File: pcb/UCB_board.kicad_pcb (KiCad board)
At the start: 4 copper layers, 160 x 100 mm, 159 parts, among them IC1 SN65HVD75DR, J1 DIN41612_02x32_AC, J2 TC2030, J3 Conn_01x02_Pin, T1 H1102NL, U1 W5500, U2 LM4040DBZ-3, U3 USBLC6-2SC6, U4 USBLC6-2SC6, U5 USBLC6-2SC6, U6 FM24C64B, U7 STM32H563VITx, Y1 3225-25M-SR, Y2 3225-25M-SR

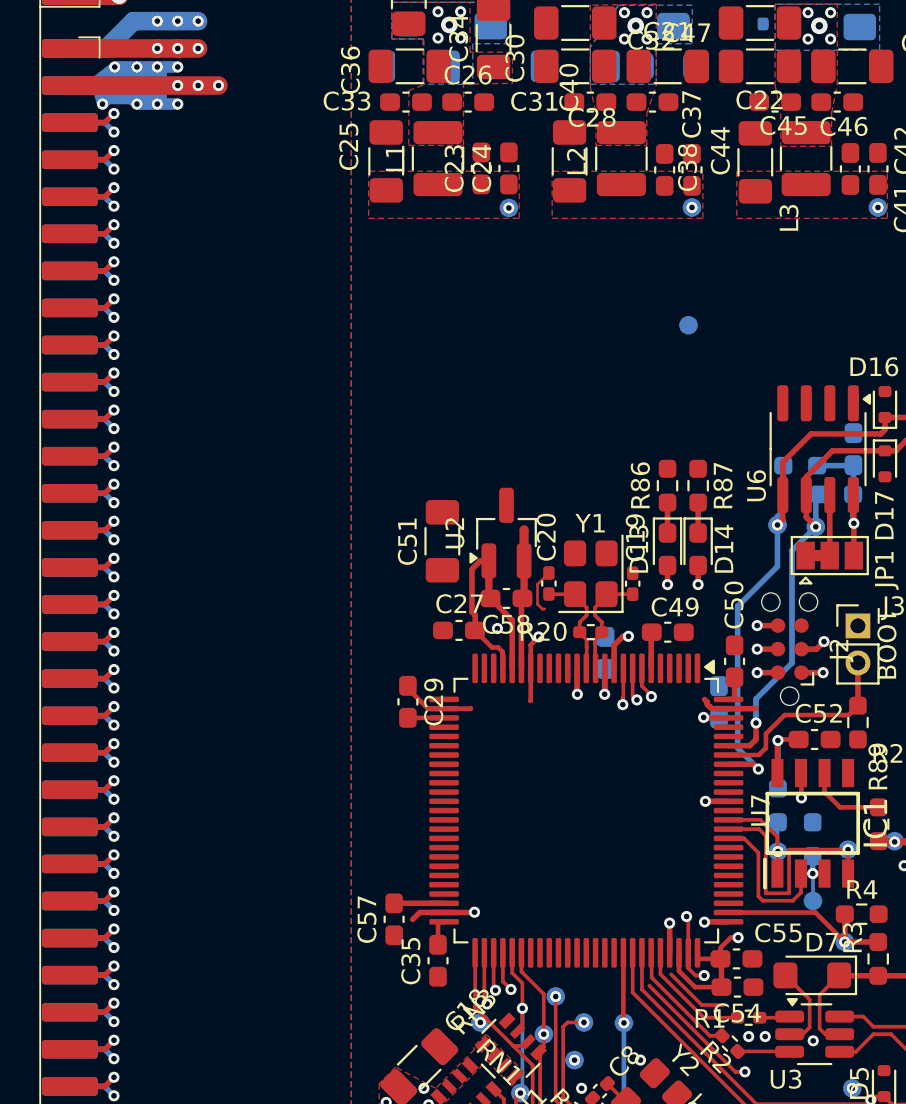
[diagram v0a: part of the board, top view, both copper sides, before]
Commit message: UniConnector new traces
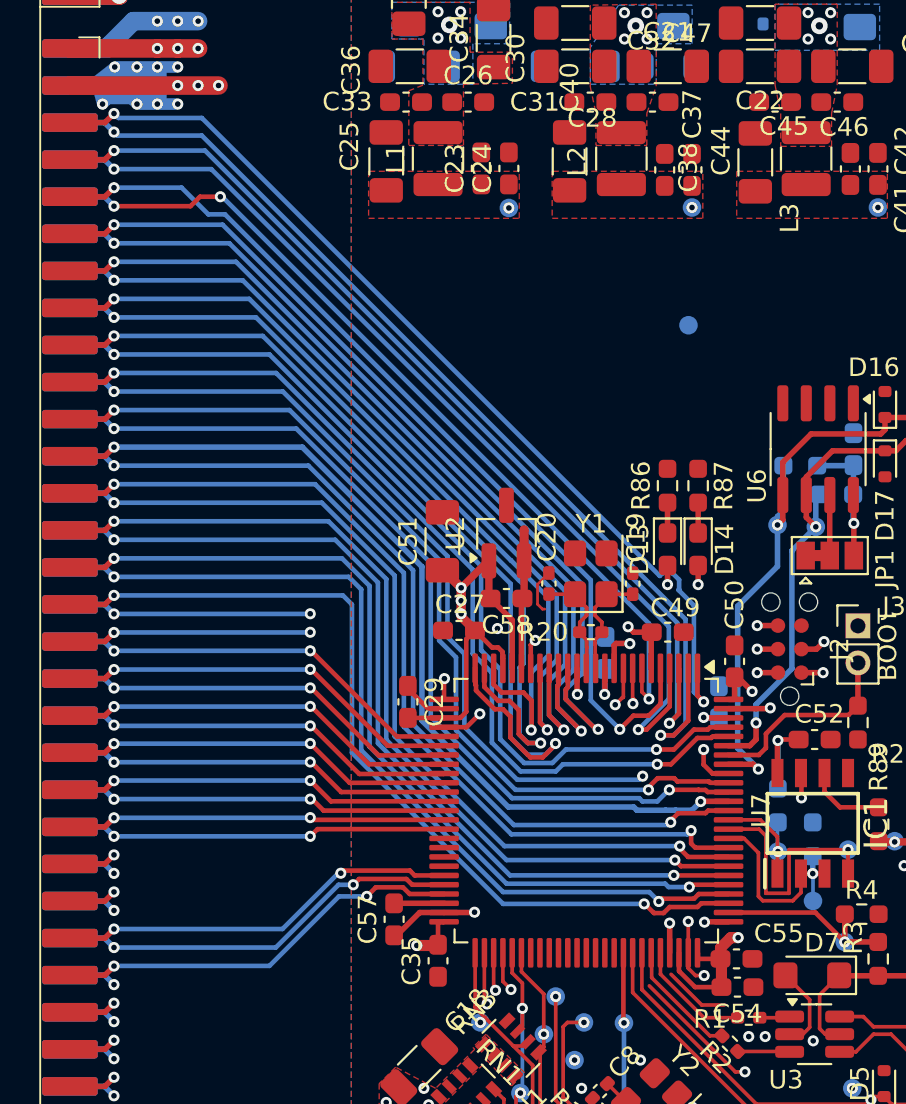
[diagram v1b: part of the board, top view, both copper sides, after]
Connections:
- net /UniConnector/IO_48 renamed /MCU/IO_48
- net /UniConnector/IO_49 renamed /MCU/IO_49
- net /UniConnector/IO_50 renamed /MCU/IO_50
- net /UniConnector/IO_51 renamed /MCU/IO_51
- net /UniConnector/IO_52 renamed /MCU/IO_52
- net /UniConnector/IO_53 renamed /MCU/IO_53
- net /UniConnector/IO_54 renamed /MCU/IO_54
- net /UniConnector/IO_55 renamed /MCU/IO_55
- net /UniConnector/IO_56 renamed /MCU/IO_56
- net /UniConnector/IO_57 renamed /MCU/IO_57
- net /UniConnector/IO_58 renamed /MCU/IO_58
- net /UniConnector/IO_59 renamed /MCU/IO_59
- net /UniConnector/IO_60 renamed /MCU/IO_60
- net /UniConnector/IO_61 renamed /MCU/IO_61
- net /UniConnector/IO_62 renamed /MCU/IO_62
- net /UniConnector/IO_63 renamed /MCU/IO_63
- net /UniConnector/IO_64 renamed /MCU/IO_64
- net /UniConnector/IO_65 renamed /MCU/IO_65
- net /UniConnector/IO_66 renamed /MCU/IO_66
- net /UniConnector/IO_67 renamed /MCU/IO_67
- net /UniConnector/IO_68 renamed /MCU/IO_68
- net /UniConnector/IO_69 renamed /MCU/IO_69
- net /UniConnector/IO_70 renamed /MCU/IO_70
- net /UniConnector/IO_71 renamed /MCU/IO_71
- net /UniConnector/IO_72 renamed /MCU/IO_72
- net /UniConnector/IO_73 renamed /MCU/IO_73
- net /UniConnector/IO_74 renamed /MCU/IO_74
- net /UniConnector/IO_75 renamed /MCU/IO_75
- net /UniConnector/IO_76 renamed /MCU/IO_76
- J2 pad 4: /MCU/IO_20 -> /MCU/IO_19
- U7 pad 26: /MCU/IO_14 -> /MCU/IO_28
- U7 pad 29: unconnected-(U7-PA4-Pad29) -> /MCU/IO_29
- U7 pad 30: unconnected-(U7-PA5-Pad30) -> /MCU/IO_30
- U7 pad 31: unconnected-(U7-PA6-Pad31) -> /MCU/IO_31
- U7 pad 32: unconnected-(U7-PA7-Pad32) -> /MCU/IO_32
- U7 pad 33: unconnected-(U7-PC4-Pad33) -> /MCU/IO_33
- U7 pad 34: unconnected-(U7-PC5-Pad34) -> /MCU/IO_34
- U7 pad 35: unconnected-(U7-PB0-Pad35) -> /MCU/IO_35
- U7 pad 36: unconnected-(U7-PB1-Pad36) -> /MCU/IO_36
- U7 pad 37: unconnected-(U7-PB2-Pad37) -> /MCU/IO_37
- U7 pad 38: unconnected-(U7-PE7-Pad38) -> /MCU/IO_38
- U7 pad 39: unconnected-(U7-PE8-Pad39) -> /MCU/IO_39
- U7 pad 40: unconnected-(U7-PE9-Pad40) -> /MCU/IO_40
- U7 pad 41: unconnected-(U7-PE10-Pad41) -> /MCU/IO_41
- U7 pad 42: unconnected-(U7-PE11-Pad42) -> /MCU/IO_42
- U7 pad 43: unconnected-(U7-PE12-Pad43) -> /MCU/IO_43
- U7 pad 44: unconnected-(U7-PE13-Pad44) -> /MCU/IO_44
- U7 pad 45: unconnected-(U7-PE14-Pad45) -> /MCU/IO_45
- U7 pad 46: unconnected-(U7-PE15-Pad46) -> /MCU/IO_46
- U7 pad 47: unconnected-(U7-PB10-Pad47) -> /MCU/IO_47
- U7 pad 78: /MCU/IO_28 -> /MCU/IO_27
- U7 pad 79: /MCU/IO_27 -> /MCU/IO_26
- U7 pad 80: /MCU/IO_26 -> /MCU/IO_25
- U7 pad 81: /MCU/IO_25 -> /MCU/IO_24
- U7 pad 82: /MCU/IO_24 -> /MCU/IO_23
- U7 pad 83: /MCU/IO_23 -> /MCU/IO_22
- U7 pad 84: /MCU/IO_22 -> /MCU/IO_21
- U7 pad 88: /MCU/IO_21 -> /MCU/IO_20
- U7 pad 89: /MCU/IO_20 -> /MCU/IO_19
- U7 pad 90: /MCU/IO_19 -> /MCU/IO_18
- U7 pad 91: /MCU/IO_18 -> /MCU/IO_17
- U7 pad 92: /MCU/IO_17 -> /MCU/IO_16
- U7 pad 96: /MCU/IO_16 -> /MCU/IO_15
- U7 pad 97: /MCU/IO_15 -> /MCU/IO_14
- X1 pad 10: /UniConnector/IO_6 -> /MCU/IO_6
- X1 pad 11: /UniConnector/IO_7 -> /MCU/IO_7
- X1 pad 12: /UniConnector/IO_8 -> /MCU/IO_8
- X1 pad 13: /UniConnector/IO_9 -> /MCU/IO_9
- X1 pad 14: /UniConnector/IO_10 -> /MCU/IO_10
- X1 pad 15: /UniConnector/IO_11 -> /MCU/IO_11
- X1 pad 16: /UniConnector/IO_12 -> /MCU/IO_12
- X1 pad 17: /UniConnector/IO_13 -> /MCU/IO_13
- X1 pad 18: /UniConnector/IO_14 -> /MCU/IO_14
- X1 pad 19: /UniConnector/IO_15 -> /MCU/IO_15
- X1 pad 20: /UniConnector/IO_16 -> /MCU/IO_16
- X1 pad 21: /UniConnector/IO_17 -> /MCU/IO_17
- X1 pad 22: /UniConnector/IO_18 -> /MCU/IO_18
- X1 pad 23: /UniConnector/IO_19 -> /MCU/IO_19
- X1 pad 24: /UniConnector/IO_20 -> /MCU/IO_20
- X1 pad 25: /UniConnector/IO_21 -> /MCU/IO_21
- X1 pad 26: /UniConnector/IO_22 -> /MCU/IO_22
- X1 pad 27: /UniConnector/IO_23 -> /MCU/IO_23
- X1 pad 28: /UniConnector/IO_24 -> /MCU/IO_24
- X1 pad 29: /UniConnector/IO_25 -> /MCU/IO_25
- X1 pad 30: /UniConnector/IO_26 -> /MCU/IO_26
- X1 pad 31: /UniConnector/IO_27 -> /MCU/IO_27
- X1 pad 32: /UniConnector/IO_28 -> /MCU/IO_28
- X1 pad 33: /UniConnector/IO_29 -> /MCU/IO_29
- X1 pad 34: /UniConnector/IO_30 -> /MCU/IO_30
- X1 pad 35: /UniConnector/IO_31 -> /MCU/IO_31
- X1 pad 36: /UniConnector/IO_32 -> /MCU/IO_32
- X1 pad 37: /UniConnector/IO_33 -> /MCU/IO_33
- X1 pad 38: /UniConnector/IO_34 -> /MCU/IO_34
- X1 pad 39: /UniConnector/IO_35 -> /MCU/IO_35
- X1 pad 40: /UniConnector/IO_36 -> /MCU/IO_36
- X1 pad 41: /UniConnector/IO_37 -> /MCU/IO_37
- X1 pad 42: /UniConnector/IO_38 -> /MCU/IO_38
- X1 pad 43: /UniConnector/IO_39 -> /MCU/IO_39
- X1 pad 44: /UniConnector/IO_40 -> /MCU/IO_40
- X1 pad 45: /UniConnector/IO_41 -> /MCU/IO_41
- X1 pad 46: /UniConnector/IO_42 -> /MCU/IO_42
- X1 pad 47: /UniConnector/IO_43 -> /MCU/IO_43
- X1 pad 48: /UniConnector/IO_44 -> /MCU/IO_44
- X1 pad 49: /UniConnector/IO_45 -> /MCU/IO_45
- X1 pad 5: /UniConnector/IO_1 -> /MCU/IO_1
- X1 pad 50: /UniConnector/IO_46 -> /MCU/IO_46
- X1 pad 51: /UniConnector/IO_47 -> /MCU/IO_47
- X1 pad 6: /UniConnector/IO_2 -> /MCU/IO_2
- X1 pad 7: /UniConnector/IO_3 -> /MCU/IO_3
- X1 pad 8: /UniConnector/IO_4 -> /MCU/IO_4
- X1 pad 9: /UniConnector/IO_5 -> /MCU/IO_5
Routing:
- net +3.3V: track 129.3 -> 205.6 mm, vias 24 -> 30
- net /MCU/IO_19: track 0.00 -> 60.7 mm, vias 0 -> 3
- net /MCU/IO_2: track 0.00 -> 56.2 mm, vias 0 -> 2
- net /MCU/IO_4: track 0.00 -> 53.3 mm, vias 0 -> 2
- net /MCU/IO_1: track 0.00 -> 52.7 mm, vias 0 -> 2
- net /MCU/IO_3: track 0.00 -> 52.3 mm, vias 0 -> 2
- net /MCU/IO_16: track 0.00 -> 51.0 mm, vias 0 -> 3
- net /MCU/IO_14: track 0.00 -> 50.5 mm, vias 0 -> 2
- net /MCU/IO_5: track 0.00 -> 50.5 mm, vias 0 -> 2
- net /MCU/IO_15: track 0.00 -> 50.3 mm, vias 0 -> 2
- net /MCU/IO_17: track 0.00 -> 49.5 mm, vias 0 -> 2
- net /MCU/IO_21: track 0.00 -> 49.3 mm, vias 0 -> 2
- net /MCU/IO_18: track 0.00 -> 49.3 mm, vias 0 -> 2
- net /MCU/IO_7: track 0.00 -> 49.0 mm, vias 0 -> 2
- net /MCU/IO_13: track 0.00 -> 48.9 mm, vias 0 -> 2
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
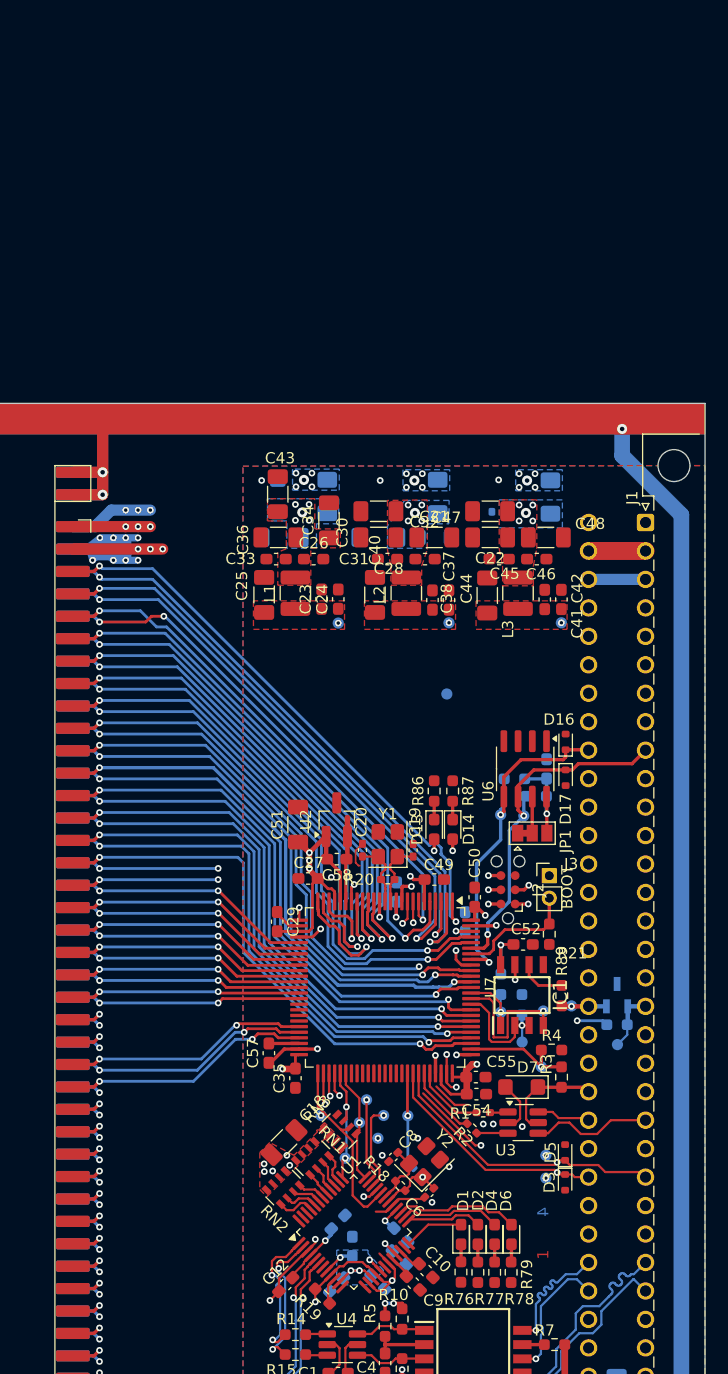
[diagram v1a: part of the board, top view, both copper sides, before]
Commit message: Added SI5351C
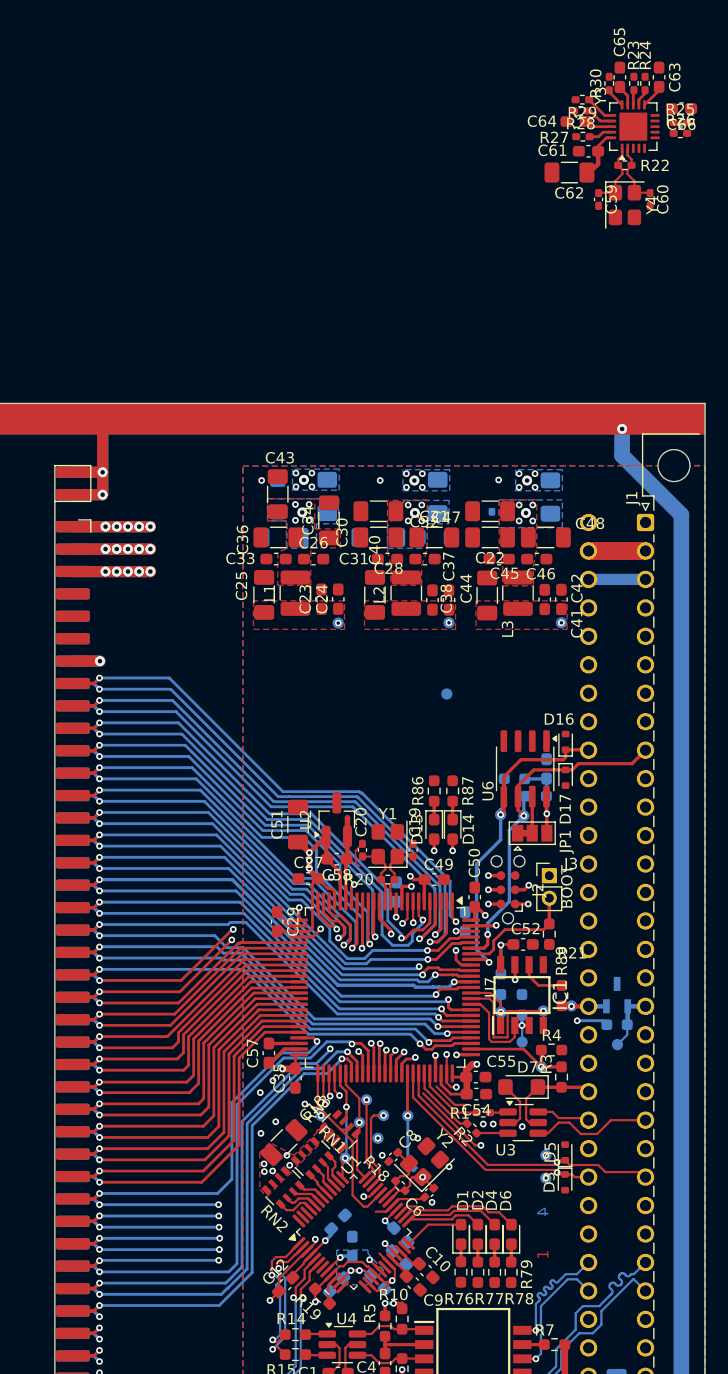
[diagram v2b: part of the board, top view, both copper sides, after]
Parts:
- added C59: 18p, Capacitor_SMD:C_0402_1005Metric_Pad0.74x0.62mm_HandSolder, F.Cu at (220.5, 31.8)
- added C60: 18p, Capacitor_SMD:C_0402_1005Metric_Pad0.74x0.62mm_HandSolder, F.Cu at (225.1, 31.8)
- added C61: 100n, Capacitor_SMD:C_0603_1608Metric_Pad1.08x0.95mm_HandSolder, F.Cu at (219.6, 27.5)
- added C62: 10u, Capacitor_SMD:C_1206_3216Metric_Pad1.33x1.80mm_HandSolder, F.Cu at (217.9, 29.4)
- added C63: 100n, Capacitor_SMD:C_0603_1608Metric_Pad1.08x0.95mm_HandSolder, F.Cu at (225.9, 20.9)
- added C64: 100n, Capacitor_SMD:C_0603_1608Metric_Pad1.08x0.95mm_HandSolder, F.Cu at (218.5, 24.8)
- added C65: 100n, Capacitor_SMD:C_0603_1608Metric_Pad1.08x0.95mm_HandSolder, F.Cu at (222.4, 20.9)
- added C66: 100n, Capacitor_SMD:C_0603_1608Metric_Pad1.08x0.95mm_HandSolder, F.Cu at (227.9, 23.7)
- added R22: 1M, Resistor_SMD:R_0402_1005Metric_Pad0.72x0.64mm_HandSolder, F.Cu at (222.9, 28.7)
- added R23: 0R, Resistor_SMD:R_0402_1005Metric_Pad0.72x0.64mm_HandSolder, F.Cu at (223.7, 21.4)
- added R24: 0R, Resistor_SMD:R_0402_1005Metric_Pad0.72x0.64mm_HandSolder, F.Cu at (224.7, 21.4)
- added R25: 0R, Resistor_SMD:R_0402_1005Metric_Pad0.72x0.64mm_HandSolder, F.Cu at (227.8, 24.9)
- added R26: 0R, Resistor_SMD:R_0402_1005Metric_Pad0.72x0.64mm_HandSolder, F.Cu at (227.8, 25.9)
- added R27: 0R, Resistor_SMD:R_0402_1005Metric_Pad0.72x0.64mm_HandSolder, F.Cu at (219.1, 26.2)
- added R28: 0R, Resistor_SMD:R_0402_1005Metric_Pad0.72x0.64mm_HandSolder, F.Cu at (218.9, 23.9)
- added R29: 0R, Resistor_SMD:R_0402_1005Metric_Pad0.72x0.64mm_HandSolder, F.Cu at (219.1, 22.9)
- added R30: 0R, Resistor_SMD:R_0402_1005Metric_Pad0.72x0.64mm_HandSolder, F.Cu at (221.5, 21.4)
- added Y3: Si5351C-B-GM, Package_DFN_QFN:QFN-20-1EP_4x4mm_P0.5mm_EP2.5x2.5mm, F.Cu at (223.6, 25.3)
- added Y4: 3225-25M-SR, Crystal:Crystal_SMD_3225-4Pin_3.2x2.5mm, F.Cu at (222.9, 32.3)
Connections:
- J1 pad c7: /ConnectorDIN41612/CLK_IN -> /Clock/CLK_IN
- R80 pad 1: /EthernetPHY/CLKIN -> Net-(U7-PA8)
- TP12 pad 1: /EthernetPHY/CLKIN -> /EthernetPHY/XO+
- U7 pad 57: unconnected-(U7-PD10-Pad57) -> /MCU/IO_57
- U7 pad 58: unconnected-(U7-PD11-Pad58) -> /MCU/IO_56
- U7 pad 59: unconnected-(U7-PD12-Pad59) -> /MCU/IO_55
- U7 pad 60: unconnected-(U7-PD13-Pad60) -> /MCU/IO_54
- U7 pad 61: unconnected-(U7-PD14-Pad61) -> /MCU/IO_53
- U7 pad 62: unconnected-(U7-PD15-Pad62) -> /MCU/IO_52
- U7 pad 63: unconnected-(U7-PC6-Pad63) -> /MCU/IO_51
- U7 pad 64: unconnected-(U7-PC7-Pad64) -> /MCU/IO_50
- U7 pad 65: unconnected-(U7-PC8-Pad65) -> /MCU/IO_49
- U7 pad 66: unconnected-(U7-PC9-Pad66) -> /MCU/IO_48
- U7 pad 67: /EthernetPHY/CLKIN -> Net-(U7-PA8)
- X1 pad 10: /MCU/IO_6 -> GND
- X1 pad 11: /MCU/IO_7 -> CLK_IN2
- X1 pad 12: /MCU/IO_8 -> GND
- X1 pad 13: /MCU/IO_9 -> GND
- X1 pad 14: /MCU/IO_10 -> GND
- X1 pad 15: /MCU/IO_11 -> /MCU/IO_1
- X1 pad 16: /MCU/IO_12 -> /MCU/IO_2
- X1 pad 17: /MCU/IO_13 -> /MCU/IO_3
- X1 pad 18: /MCU/IO_14 -> /MCU/IO_4
- X1 pad 19: /MCU/IO_15 -> /MCU/IO_5
- X1 pad 2: +5V -> +12V
- X1 pad 20: /MCU/IO_16 -> /MCU/IO_6
- X1 pad 21: /MCU/IO_17 -> /MCU/IO_7
- X1 pad 22: /MCU/IO_18 -> /MCU/IO_8
- X1 pad 23: /MCU/IO_19 -> /MCU/IO_9
- X1 pad 24: /MCU/IO_20 -> /MCU/IO_10
- X1 pad 25: /MCU/IO_21 -> /MCU/IO_11
- X1 pad 26: /MCU/IO_22 -> /MCU/IO_12
- X1 pad 27: /MCU/IO_23 -> /MCU/IO_13
- X1 pad 28: /MCU/IO_24 -> /MCU/IO_14
- X1 pad 29: /MCU/IO_25 -> /MCU/IO_15
- X1 pad 3: +3.3V -> +5V
- X1 pad 30: /MCU/IO_26 -> /MCU/IO_16
- X1 pad 31: /MCU/IO_27 -> /MCU/IO_17
- X1 pad 32: /MCU/IO_28 -> /MCU/IO_18
- X1 pad 33: /MCU/IO_29 -> /MCU/IO_19
- X1 pad 34: /MCU/IO_30 -> /MCU/IO_20
- X1 pad 35: /MCU/IO_31 -> /MCU/IO_21
- X1 pad 36: /MCU/IO_32 -> /MCU/IO_22
- X1 pad 37: /MCU/IO_33 -> /MCU/IO_23
- X1 pad 38: /MCU/IO_34 -> /MCU/IO_24
- X1 pad 39: /MCU/IO_35 -> /MCU/IO_25
- X1 pad 4: GND -> +5V
- X1 pad 40: /MCU/IO_36 -> /MCU/IO_26
- X1 pad 41: /MCU/IO_37 -> /MCU/IO_27
- X1 pad 42: /MCU/IO_38 -> /MCU/IO_28
- X1 pad 43: /MCU/IO_39 -> /MCU/IO_29
- X1 pad 44: /MCU/IO_40 -> /MCU/IO_30
- X1 pad 45: /MCU/IO_41 -> /MCU/IO_31
- X1 pad 46: /MCU/IO_42 -> /MCU/IO_32
- X1 pad 47: /MCU/IO_43 -> /MCU/IO_33
- X1 pad 48: /MCU/IO_44 -> /MCU/IO_34
- X1 pad 49: /MCU/IO_45 -> /MCU/IO_35
- X1 pad 5: /MCU/IO_1 -> +3.3V
- X1 pad 50: /MCU/IO_46 -> /MCU/IO_36
- X1 pad 51: /MCU/IO_47 -> /MCU/IO_37
- X1 pad 52: /MCU/IO_48 -> /MCU/IO_38
- X1 pad 53: /MCU/IO_49 -> /MCU/IO_39
- X1 pad 54: /MCU/IO_50 -> /MCU/IO_40
- X1 pad 55: /MCU/IO_51 -> /MCU/IO_41
- X1 pad 56: /MCU/IO_52 -> /MCU/IO_42
- X1 pad 57: /MCU/IO_53 -> /MCU/IO_43
- X1 pad 58: /MCU/IO_54 -> /MCU/IO_44
- X1 pad 59: /MCU/IO_55 -> /MCU/IO_45
- X1 pad 6: /MCU/IO_2 -> +3.3V
- X1 pad 60: /MCU/IO_56 -> /MCU/IO_46
- X1 pad 61: /MCU/IO_57 -> /MCU/IO_47
- X1 pad 62: /MCU/IO_58 -> /MCU/IO_48
- X1 pad 63: /MCU/IO_59 -> /MCU/IO_49
- X1 pad 64: /MCU/IO_60 -> /MCU/IO_50
- X1 pad 65: /MCU/IO_61 -> /MCU/IO_51
- X1 pad 66: /MCU/IO_62 -> /MCU/IO_52
- X1 pad 67: /MCU/IO_63 -> /MCU/IO_53
- X1 pad 68: /MCU/IO_64 -> /MCU/IO_54
- X1 pad 69: /MCU/IO_65 -> /MCU/IO_55
- X1 pad 7: /MCU/IO_3 -> GND
- X1 pad 70: /MCU/IO_66 -> /MCU/IO_56
- X1 pad 71: /MCU/IO_67 -> /MCU/IO_57
- X1 pad 72: /MCU/IO_68 -> unconnected-(X1-Pad72)
- X1 pad 73: /MCU/IO_69 -> unconnected-(X1-Pad73)
- X1 pad 74: /MCU/IO_70 -> unconnected-(X1-Pad74)
- X1 pad 75: /MCU/IO_71 -> unconnected-(X1-Pad75)
- X1 pad 76: /MCU/IO_72 -> unconnected-(X1-Pad76)
- X1 pad 77: /MCU/IO_73 -> unconnected-(X1-Pad77)
- X1 pad 78: /MCU/IO_74 -> unconnected-(X1-Pad78)
- X1 pad 79: /MCU/IO_75 -> unconnected-(X1-Pad79)
- X1 pad 8: /MCU/IO_4 -> GND
- X1 pad 80: /MCU/IO_76 -> unconnected-(X1-Pad80)
- X1 pad 9: /MCU/IO_5 -> CLK_IN1
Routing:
- net /MCU/IO_48: track 2.59 -> 50.2 mm, vias 1 -> 3
- net /MCU/IO_49: track 2.58 -> 49.2 mm, vias 1 -> 3
- net /MCU/IO_50: track 2.59 -> 48.6 mm, vias 1 -> 3
- net /MCU/IO_51: track 2.58 -> 48.3 mm, vias 1 -> 3
- net /MCU/IO_52: track 2.59 -> 48.3 mm, vias 1 -> 3
- net /MCU/IO_53: track 2.58 -> 47.1 mm, vias 1 -> 3
- net /MCU/IO_55: track 2.58 -> 46.1 mm, vias 1 -> 3
- net /MCU/IO_54: track 2.59 -> 45.8 mm, vias 1 -> 2
- net /MCU/IO_56: track 2.59 -> 43.6 mm, vias 1 -> 2
- net /MCU/IO_57: track 2.58 -> 42.9 mm, vias 1 -> 2
- net /MCU/IO_44: track 2.59 -> 29.8 mm
- net /MCU/IO_43: track 2.58 -> 29.5 mm
- net /MCU/IO_42: track 2.59 -> 29.2 mm
- net /MCU/IO_41: track 2.58 -> 28.5 mm
- net +3.3V: track 205.6 -> 225.5 mm, vias 30 -> 32
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
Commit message: Clock rounting
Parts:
- removed R27, R28, R29, R30: 0R, Resistor_SMD:R_0402_1005Metric_Pad0.72x0.64mm_HandSolder
- R23, R24: moved to B.Cu
- moved R23 94.0 mm to (202.9, 113.1)
- moved R24 71.7 mm to (201.0, 89.1)
- moved C65 64.1 mm to (194.6, 78.6), turned to 0 degrees
- moved C63 62.6 mm to (194.6, 75.1), turned to 0 degrees
- moved C66 60.0 mm to (194.6, 73.6), turned to 0 degrees
- moved C64 59.8 mm to (197.7, 80.9)
- moved Y3 57.7 mm to (199.0, 77.4), turned to 180 degrees
- moved R25 56.9 mm to (198.4, 73.6), turned to -90 degrees
- moved C61 56.6 mm to (201.0, 80.9), turned to 180 degrees
- moved C62 56.0 mm to (201.1, 82.8), turned to 0 degrees
- moved R26 55.5 mm to (199.4, 73.6), turned to -90 degrees
- moved R22 53.5 mm to (202.4, 78.2), turned to 90 degrees
- moved C59 51.0 mm to (205.5, 80.5), turned to 0 degrees
- moved Y4 48.9 mm to (206.0, 78.2), turned to 0 degrees
- moved C60 48.3 mm to (205.5, 75.9), turned to 0 degrees
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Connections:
- R23 pad 1: Net-(Y3-CLK0) -> /EthernetPHY/XO+
- R23 pad 2: /EthernetPHY/XO+ -> /Clock/CLK0
- R24 pad 1: Net-(Y3-CLK1) -> /MCU/XTAL+
- R24 pad 2: /MCU/XTAL+ -> /Clock/CLK1
- R25 pad 1: Net-(Y3-CLK2) -> /UniConnector/CLK_IN1
- R26 pad 1: Net-(Y3-CLK3) -> /UniConnector/CLK_IN2
- X1 pad 11: CLK_IN2 -> /UniConnector/CLK_IN1
- X1 pad 9: CLK_IN1 -> /UniConnector/CLK_IN2
- Y3 pad 12: Net-(Y3-CLK1) -> /Clock/CLK1
- Y3 pad 13: Net-(Y3-CLK0) -> /Clock/CLK0
- Y3 pad 15: Net-(Y3-CLK7) -> /Clock/CLK7
- Y3 pad 16: Net-(Y3-CLK6) -> /Clock/CLK6
- Y3 pad 17: Net-(Y3-CLK5) -> /Clock/CLK5
- Y3 pad 19: Net-(Y3-CLK4) -> /Clock/CLK4
- Y3 pad 8: Net-(Y3-CLK3) -> /Clock/CLK3
- Y3 pad 9: Net-(Y3-CLK2) -> /Clock/CLK2
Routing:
- net /Clock/CLK0: track 0.00 -> 41.3 mm, vias 0 -> 2
- net +3.3V: track 225.5 -> 261.4 mm, vias 32 -> 35
- net /UniConnector/CLK_IN1: track 0.00 -> 27.8 mm
- net /UniConnector/CLK_IN2: track 0.00 -> 27.5 mm
- net /Clock/CLK_IN: track 0.00 -> 20.8 mm
- net GND: track 74.9 -> 92.5 mm, vias 29 -> 35
- net /Clock/CLK1: track 0.00 -> 16.1 mm, vias 0 -> 2
- net Net-(U7-PA8): track 0.00 -> 2.97 mm, vias 0 -> 1
- net Net-(Y3-CLK6): track 2.59 -> 0.00 mm
- net Net-(Y3-CLK5): track 2.54 -> 0.00 mm
- net Net-(Y3-CLK4): track 2.13 -> 0.00 mm
- net /MCU/XTAL+: track 5.99 -> 7.90 mm, vias 0 -> 1
- net Net-(Y3-CLK7): track 1.79 -> 0.00 mm
- net /EthernetPHY/XO+: track 14.3 -> 12.5 mm, vias 2 -> 1
- net Net-(Y3-CLK1): track 1.54 -> 0.00 mm
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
